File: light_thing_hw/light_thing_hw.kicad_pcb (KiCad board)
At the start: 2 copper layers, 50 x 50 mm, 53 parts, among them J1 CONNECTORS, J2 Li-Ion Battery, J3 ADDR_LED_PANEL_1_CONNECTORS, J4 ADDR_LED_PANEL_2_CONNECTORS, Q1 MMBF170, SW1 ST_USER_BUTTON1, SW2 ST_RESET_BUTTON, U1 BC832-V1, U2 LSM6DS3, U3 MCP73833T-FCI_UN, U4 LMR62421XMF, U5 LP38511MRX, U5A1 STM32L452RETx

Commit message: about to do routing
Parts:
- moved C2 3.51 mm to (138.5, 72.9)
- moved U5A1 2.45 mm to (130.1, 77.7)
- moved C1 2.45 mm to (125.5, 70.3)
- moved C3 2.45 mm to (134.8, 85.2)
- moved C4 2.45 mm to (127.8, 85.2)
- moved R11 2.45 mm to (139.1, 77.1)
- moved R5 2.45 mm to (131.6, 70.3)
- moved C7 2.45 mm to (127.8, 87.0)
- moved R10 2.45 mm to (139.1, 75.5)
- moved R12 2.45 mm to (134.8, 87.0)
- moved R13 2.45 mm to (138.4, 85.9)
- moved C16 2.31 mm to (122.5, 75.4)
- moved C17 2.22 mm to (122.5, 80.6)
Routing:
- net ADDR_LED_PANEL_1_PWM: track 31.9 -> 18.8 mm
- net CHARGER_STAT1: track 0.00 -> 2.17 mm, vias 0 -> 1
- net CHARGER_STAT2: track 0.00 -> 1.82 mm, vias 0 -> 1
- net BOOST_ENABLE: track 0.00 -> 1.76 mm, vias 0 -> 1
- net BT_GPIO_1: track 0.00 -> 1.71 mm, vias 0 -> 1
- net BT_RX: track 0.00 -> 1.67 mm, vias 0 -> 1
- net ACCEL_EXTI_1: track 0.00 -> 1.67 mm, vias 0 -> 1
- net BT_GPIO_3: track 0.00 -> 1.65 mm, vias 0 -> 1
- net D-: track 0.00 -> 1.64 mm, vias 0 -> 1
- net BATT_ADC_ENABLE: track 0.00 -> 1.61 mm, vias 0 -> 1
- net GREEN_LED: track 0.00 -> 1.59 mm, vias 0 -> 1
- net BUTTON1: track 4.42 -> 5.91 mm, vias 0 -> 1
- net BATT_ADC: track 4.02 -> 5.49 mm, vias 0 -> 1
- net BT_GPIO_2: track 0.00 -> 1.47 mm, vias 0 -> 1
- net BT_GPIO_0: track 0.00 -> 1.47 mm, vias 0 -> 1
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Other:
- outline, holes or cut-outs redrawn

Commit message: placing modules
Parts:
- U1: value BC832-V1 -> BC832
- moved R1 74.1 mm to (127.4, 94.1), turned to 270 degrees
- moved C5 70.8 mm to (123.4, 90.2), turned to 180 degrees
- moved U3 69.2 mm to (123.4, 93.2), turned to 180 degrees
- moved C6 63.4 mm to (118.5, 92.2), turned to 0 degrees
- moved R17 62.3 mm to (118.5, 94.2), turned to 0 degrees
- moved C14 32.5 mm to (75.5, 65.2)
- moved U5 32.5 mm to (80.4, 63.7)
- moved C15 32.5 mm to (86.4, 63.5)
- moved C18 32.5 mm to (86.4, 61.7)
- moved R15 32.5 mm to (89.4, 64.4)
- moved R16 32.5 mm to (91.2, 64.4)
- moved C8 32.3 mm to (87.9, 85.3), turned to 90 degrees
- moved U4 28.9 mm to (88.9, 81.5), turned to 270 degrees
- moved L1 28.1 mm to (85.7, 83.1), turned to 90 degrees
- moved C12 26.4 mm to (90.0, 77.6), turned to 270 degrees
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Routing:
- net SWDIO: track 0.00 -> 26.3 mm
- net +3V3: track 49.1 -> 65.9 mm
- net SWCLK: track 0.00 -> 15.2 mm
- net ADDR_LED_PANEL_1_PWM: track 18.8 -> 5.58 mm
- net RESET: track 3.62 -> 12.2 mm
- net +5V: track 10.0 -> 16.2 mm
- net USART_2_RX: track 0.00 -> 2.82 mm, vias 0 -> 2
- net BT_TX: track 1.46 -> 4.23 mm, vias 1 -> 2
- net BT_SWCLK: track 0.00 -> 2.77 mm, vias 0 -> 1
- net BT_RX: track 1.67 -> 4.43 mm, vias 1 -> 2
- net USART_2_TX: track 0.00 -> 2.33 mm, vias 0 -> 2
- net +BATT: track 24.0 -> 26.3 mm
- net Net-(R5-Pad1): track 3.54 -> 1.75 mm
- net BT_SWDIO: track 0.00 -> 1.00 mm, vias 0 -> 1
- net BT_RST: track 0.00 -> 1.00 mm, vias 0 -> 1
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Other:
- board text added: "3v3 regulator"
- board text added: "boost"
- board text added: "charger"

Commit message: restarting routing
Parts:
- U1: value BC832 -> BC832-V1
- U5: value LP38511MRX -> LP38511MRX-ADJ_NOPB
- moved C15 62.0 mm to (142.4, 90.0)
- moved C18 62.0 mm to (142.4, 88.2)
- moved R16 62.0 mm to (147.2, 90.9)
- moved U5 62.0 mm to (136.4, 90.2)
- moved C14 62.0 mm to (131.5, 91.7)
- moved R15 62.0 mm to (145.4, 90.9)
- moved U2 61.0 mm to (147.5, 61.3), turned to 90 degrees
- moved C11 58.8 mm to (143.2, 62.3), turned to 180 degrees
- moved R3 46.0 mm to (133.1, 64.1), turned to 180 degrees
- moved D1 45.6 mm to (127.8, 61.7), turned to 180 degrees
- moved R4 43.8 mm to (133.1, 66.0), turned to 0 degrees
- moved L1 43.7 mm to (123.9, 61.7), turned to 0 degrees
- moved C10 43.4 mm to (129.4, 64.1), turned to 180 degrees
- moved C12 41.0 mm to (129.4, 66.0), turned to 180 degrees
- moved U4 40.2 mm to (125.5, 64.9), turned to 180 degrees
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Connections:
- J4 pad 1: GND -> TEST_GPIO0
- J4 pad 3: +5V -> TEST_GPIO1
- J4 pad 4: GND -> TEST_GPIO2
- U5A1 pad 29: Net-(U5A1-Pad29) -> TEST_GPIO2
- U5A1 pad 61: Net-(U5A1-Pad61) -> TEST_GPIO0
- U5A1 pad 62: Net-(U5A1-Pad62) -> TEST_GPIO1
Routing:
- net BT_RED_LED: track 0.00 -> 90.9 mm, vias 0 -> 2
- net BT_GPIO_0: track 1.31 -> 63.7 mm, vias 1 -> 3
- net +BATT: track 26.3 -> 85.3 mm, vias 0 -> 2
- net BT_RX: track 4.43 -> 62.3 mm, vias 2 -> 1
- net TEST_GPIO1: track 0.00 -> 55.4 mm, vias 0 -> 1
- net BT_GPIO_1: track 1.54 -> 56.8 mm, vias 1 -> 3
- net TEST_GPIO0: track 0.00 -> 52.1 mm, vias 0 -> 1
- net I2C2_SCL: track 7.16 -> 54.8 mm, vias 0 -> 3
- net BT_SWCLK: track 2.77 -> 47.1 mm, vias 1 -> 3
- net BT_TX: track 4.23 -> 48.0 mm, vias 2 -> 3
- net I2C2_SDA: track 4.49 -> 46.2 mm, vias 0 -> 3
- net ACCEL_EXTI_2: track 1.46 -> 42.1 mm
- net BOOST_ENABLE: track 1.76 -> 42.3 mm
- net +3V3: track 65.9 -> 106.1 mm, vias 1 -> 4
- net ADDR_LED_BACKUP_PWM: track 0.00 -> 38.0 mm
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
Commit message: doing well actually
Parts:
- moved R13 15.2 mm to (120.2, 83.7), turned to 0 degrees
- moved R12 13.7 mm to (119.0, 80.1), turned to 90 degrees
- moved C1 13.5 mm to (135.8, 70.8), turned to 90 degrees
- moved C7 13.2 mm to (119.0, 73.1), turned to 90 degrees
- moved C2 13.1 mm to (133.2, 83.8), turned to 0 degrees
- moved C16 12.5 mm to (130.7, 67.8), turned to 180 degrees
- moved C17 12.3 mm to (125.4, 67.8), turned to 180 degrees
- moved R10 12.2 mm to (130.6, 84.4), turned to 90 degrees
- moved R5 12.1 mm to (136.5, 73.9)
- moved R11 11.7 mm to (129.0, 84.4), turned to 90 degrees
- moved C3 11.3 mm to (120.9, 80.1), turned to 270 degrees
- moved C4 10.8 mm to (120.9, 73.1), turned to 270 degrees
- moved J1 3.71 mm to (143.8, 79.5), turned to 0 degrees
- moved J4 1.38 mm to (143.8, 73.7), turned to 0 degrees
- moved U5A1 1.36 mm to (128.4, 75.4), turned to 270 degrees
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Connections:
- J1 pad 1: USART_2_RX -> USART_2_TX
- J1 pad 2: USART_2_TX -> BT_RX
- J1 pad 3: BT_RX -> USART_2_RX
- J1 pad 6: SWDIO -> RESET
- J1 pad 7: RESET -> SWDIO
- J4 pad 1: TEST_GPIO0 -> TEST_GPIO1
- J4 pad 3: TEST_GPIO1 -> TEST_GPIO0
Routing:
- net RESET: track 33.4 -> 88.0 mm, vias 3 -> 5
- net +3V3: track 106.1 -> 60.4 mm, vias 4 -> 2
- net TEST_GPIO1: track 55.4 -> 10.1 mm, vias 1 -> 0
- net BT_GPIO_3: track 1.65 -> 46.4 mm, vias 1 -> 3
- net TEST_GPIO0: track 52.1 -> 11.2 mm, vias 1 -> 0
- net ADDR_LED_BACKUP_PWM: track 38.0 -> 0.00 mm
- net +BATT: track 85.3 -> 51.3 mm, vias 2 -> 0
- net BT_RX: track 62.3 -> 36.6 mm, vias 1 -> 2
- net BT_RED_LED: track 90.9 -> 65.4 mm
- net ACCEL_EXTI_1: track 26.2 -> 1.56 mm, vias 2 -> 1
- net BOOST_ENABLE: track 42.3 -> 18.7 mm
- net TEST_GPIO2: track 1.22 -> 24.2 mm
- net VBUS: track 4.85 -> 27.8 mm
- net BT_SWCLK: track 47.1 -> 24.3 mm, vias 3 -> 1
- net SWDIO: track 37.1 -> 14.4 mm
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
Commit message: gonna add gnd now
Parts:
- added TP1: TestPoint, TestPoint:TestPoint_Pad_D1.0mm, F.Cu at (137.2, 90.3)
- U2: footprint Package_LGA:LGA-14_3x2.5mm_P0.5mm_LayoutBorder3x4y -> footprints:LGA-14_3x2.5mm_P0.5mm_LayoutBorder3x4y_modded
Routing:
- net I2C1_SCL: track 2.48 -> 67.6 mm, vias 0 -> 3
- net +3V3: track 60.4 -> 111.7 mm, vias 2 -> 7
- net +BATT: track 51.3 -> 102.1 mm, vias 0 -> 2
- net BATT_ADC: track 5.25 -> 51.7 mm, vias 1 -> 3
- net I2C1_SDA: track 2.83 -> 40.3 mm, vias 0 -> 5
- net ADDR_LED_BACKUP_PWM: track 0.00 -> 26.6 mm, vias 0 -> 2
- net ACCEL_EXTI_1: track 1.56 -> 25.0 mm
- net ACCEL_EXTI_2: track 22.9 -> 26.5 mm
- net D+: track 25.9 -> 24.4 mm
- net I2C2_SDA: track 64.8 -> 65.7 mm
- net CHARGER_STAT2: track 22.7 -> 23.5 mm
- net I2C2_SCL: track 58.3 -> 59.1 mm
- net BOOST_ENABLE: track 18.7 -> 19.5 mm
- net GREEN_LED: vias 2 -> 1
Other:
- outline, holes or cut-outs redrawn
- net class Default: clearance 0.2 -> 0.09; via_dia 0.8 -> 0.45; via_drill 0.4 -> 0.2
- rule trace_clearance: 0.2 -> 0.09
- rule trace_min: 0.2 -> 0.1
- rule via_min_drill: 0.3 -> 0.2
- rule via_min_size: 0.4 -> 0.45

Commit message: need to go thru drc
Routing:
- net GND: track 0.00 -> 16.1 mm, vias 0 -> 5
- added copper zone on B.Cu, net GND
- added copper zone on F.Cu, net GND

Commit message: hw not lookin bad ngl
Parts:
- added gnd: TestPoint, TestPoint:TestPoint_Pad_D1.0mm, F.Cu at (151.3, 99.6)
- moved L1 15.6 mm to (136.4, 71.0)
- moved C3 15.6 mm to (133.4, 89.4)
- moved C4 15.6 mm to (133.4, 82.4)
- moved R9 15.6 mm to (127.3, 72.9)
- moved 3v3 15.6 mm to (149.7, 99.6)
- moved C1 15.6 mm to (148.3, 80.0)
- moved C10 15.6 mm to (141.9, 73.3)
- moved C11 15.6 mm to (155.7, 71.5)
- moved C12 15.6 mm to (141.9, 75.2)
- moved C13 15.6 mm to (126.4, 95.2)
- moved C14 15.6 mm to (144.0, 100.9)
- moved C15 15.6 mm to (154.9, 99.2)
- moved C16 15.6 mm to (143.2, 77.1)
- moved C17 15.6 mm to (137.9, 77.1)
- moved C18 15.6 mm to (154.9, 97.5)
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- renumbered TP1 to 3v3
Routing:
- net GND: track 16.1 -> 135.0 mm, vias 5 -> 31
- net +3V3: track 111.7 -> 160.1 mm, vias 7 -> 13
- net GREEN_LED: track 17.9 -> 18.8 mm
- net ADDR_LED_PANEL_1_PWM: track 32.4 -> 31.7 mm
- net TEST_GPIO1: track 10.1 -> 10.7 mm
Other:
- board text added: "5v"
- board text added: "JLCJLCJLCJLC"
- board text added: "RESET"
- board text added: "USER BUTTON 1"
- board text added: "accel"
- board text added: "bkup"
- board text added: "bt_reset"
- board text added: "bt_rx"
- board text added: "bt_swclk"
- board text added: "bt_swdio"
- board text added: "bt_tx"
- board text added: "gnd"
- board text added: "panel1pwm"
- board text added: "st_reset"
- board text added: "st_swclk"
- board text added: "st_swdio"
- board text added: "t0"
- board text added: "t1"
- board text added: "t2"
- board text added: "usart2_rx"
- board text added: "usart2_tx"

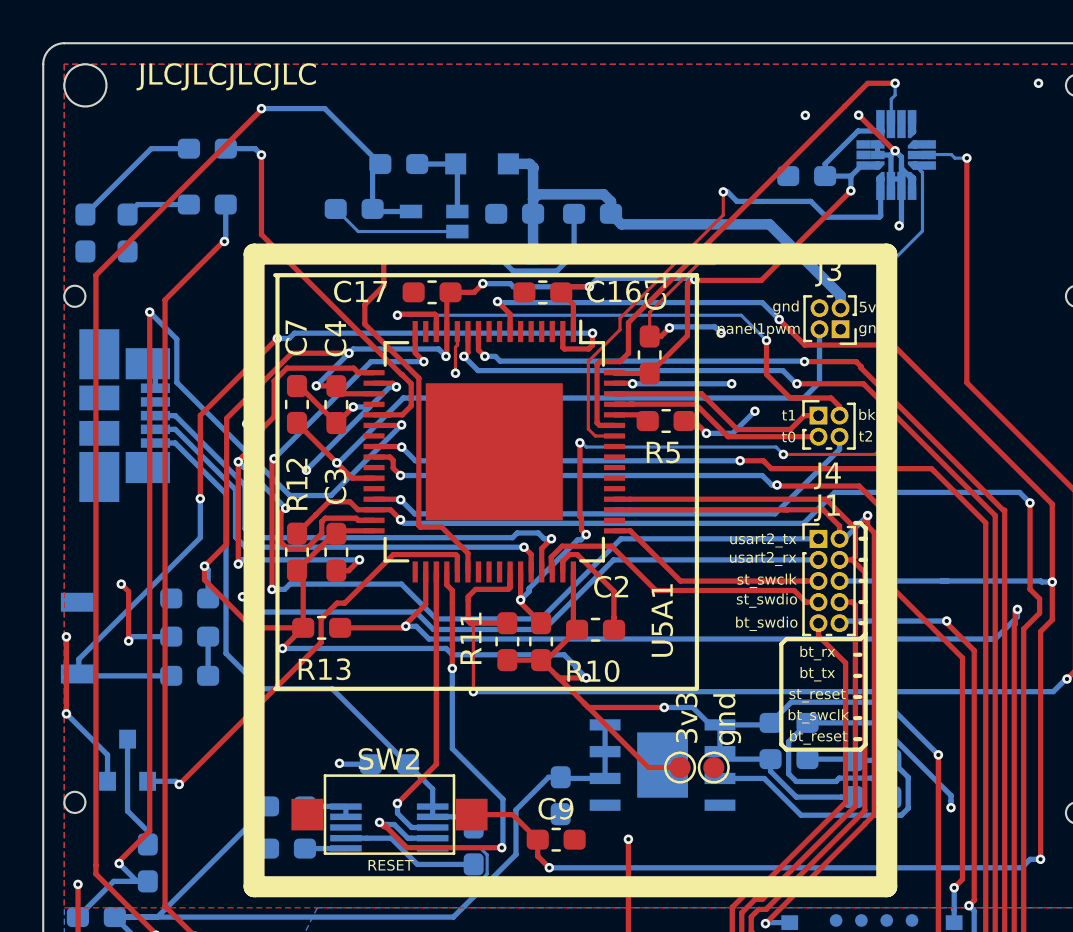
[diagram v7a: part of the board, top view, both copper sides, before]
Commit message: added MIC_IN to hardware and in stmcube
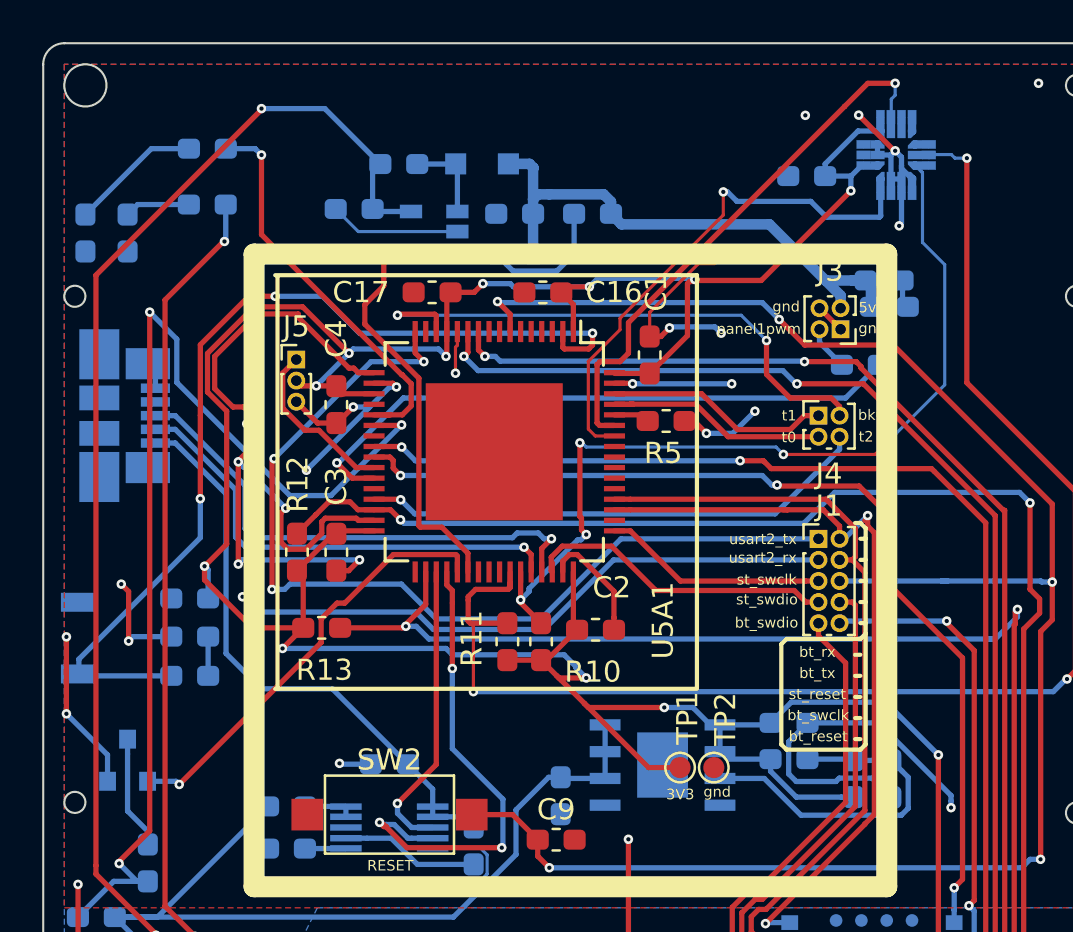
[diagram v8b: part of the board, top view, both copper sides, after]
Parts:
- added 1000uF1: C_Small, Capacitor_SMD:C_0603_1608Metric_Pad1.05x0.95mm_HandSolder, B.Cu at (159.6, 77.8)
- added J5: MIC_CONN, Connector_PinHeader_1.00mm:PinHeader_1x03_P1.00mm_Vertical, F.Cu at (131.5, 80.2)
- added R18: 300, Resistor_SMD:R_0603_1608Metric_Pad1.05x0.95mm_HandSolder, B.Cu at (158.2, 80.5)
- C7: moved to B.Cu
- moved C7 28.5 mm to (159.4, 76.5), turned to 0 degrees
- renumbered 3v3 to TP1, gnd to TP2
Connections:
- C7 pad 1: ADDR_LED_PANEL_1_PWM -> +5V
- J3 pad 2: ADDR_LED_PANEL_1_PWM -> Net-(J3-Pad2)
- U5A1 pad 26: Net-(U5A1-Pad26) -> MIC_IN
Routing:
- net MIC_IN: track 0.00 -> 8.07 mm
- net USART_2_RX: track 45.9 -> 52.4 mm
- net +3V3: track 160.1 -> 166.1 mm
- net BUTTON1: track 42.1 -> 45.5 mm
- net +5V: track 23.0 -> 26.2 mm
- net GND: track 135.0 -> 137.4 mm
- net Net-(J3-Pad2): track 0.00 -> 2.13 mm
- net ADDR_LED_PANEL_1_PWM: track 31.7 -> 29.6 mm
- net I2C1_SDA: track 40.7 -> 41.6 mm
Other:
- board text added: "3V3"
- board text added: "3v3"
- board text added: "mic_in"
